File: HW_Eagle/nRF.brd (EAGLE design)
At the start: 44.4 x 39.9 mm, 24 parts, among them X1 B4B-ZR

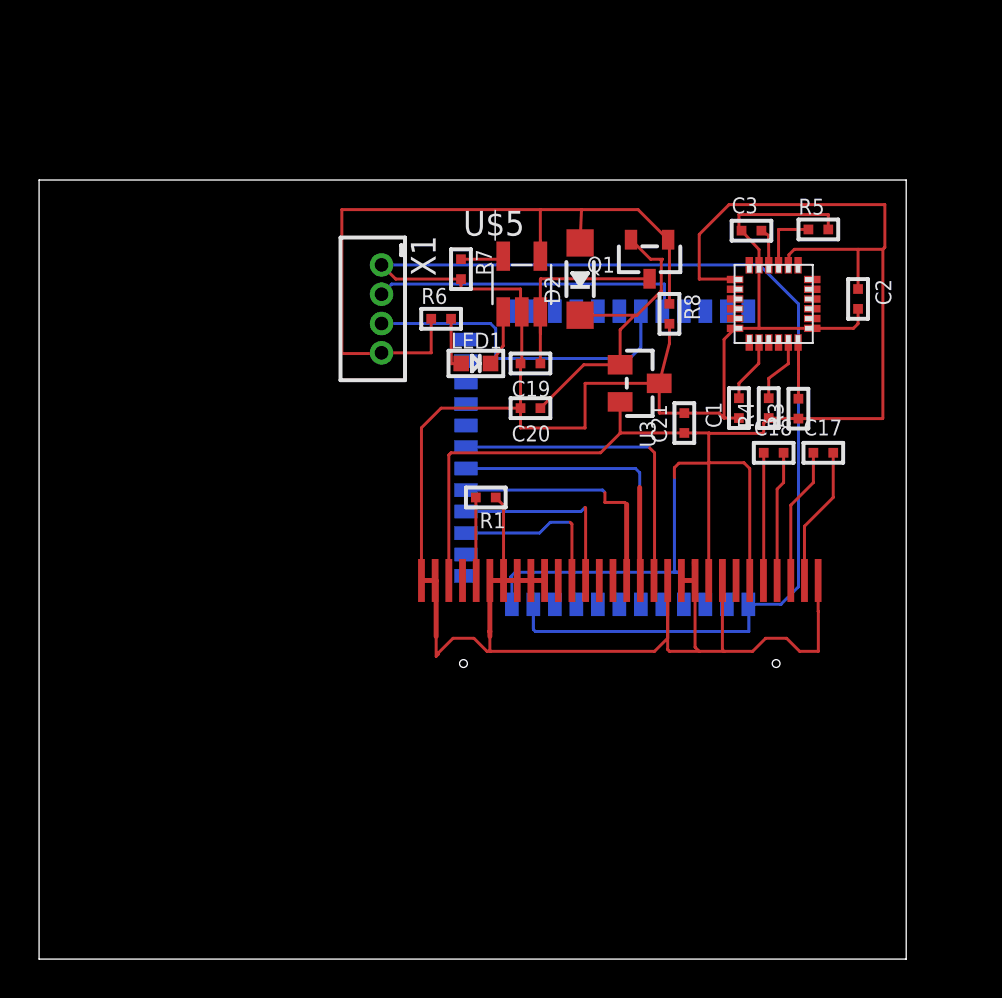
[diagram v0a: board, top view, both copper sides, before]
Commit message: [HW] Add Batterry connector
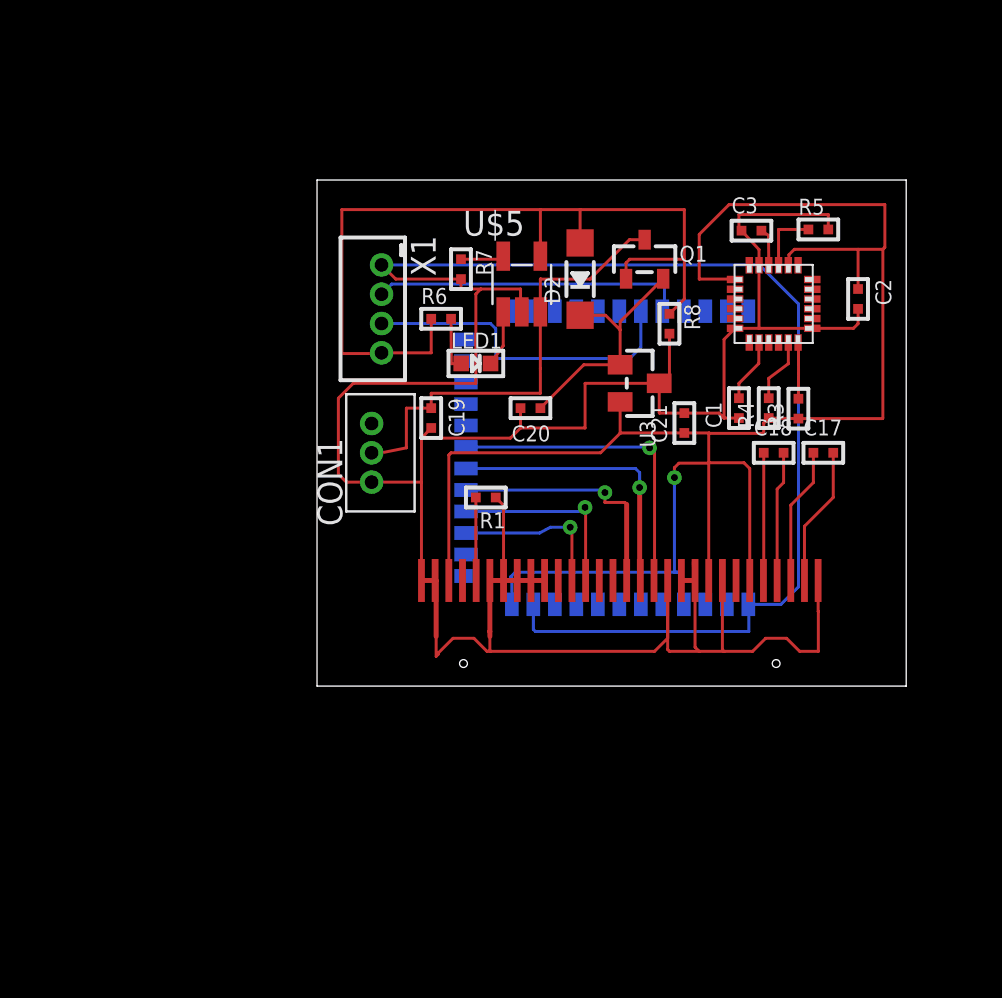
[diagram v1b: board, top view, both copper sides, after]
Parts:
- added CON1: B3B-ZR, jst:B3B-ZR
- moved C19 5.80 mm to (22.1, 55.1), turned to 270 degrees
- moved R8 0.51 mm to (34.3, 59.9)
- moved Q1 0.25 mm to (33.0, 63.2), turned to 0 degrees
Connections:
- net GND: now also CON1.1
- net VBAT: now also CON1.2
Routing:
- net GND: track 179.5 -> 194.9 mm
- net VBAT: track 11.0 -> 23.5 mm
- net N$15: track 39.2 -> 45.6 mm
- net N$25: track 16.2 -> 12.7 mm
- net MOSI: track 8.58 -> 8.48 mm, vias 0 -> 1
- net VCC: vias 0 -> 1
- net SCK: vias 0 -> 1
- net RES: vias 0 -> 1
- net DC: vias 0 -> 1
- net CS: vias 0 -> 1
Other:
- board size 44.4 x 39.9 mm -> 30.1 x 25.9 mm

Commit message: [HW] Change to using modules
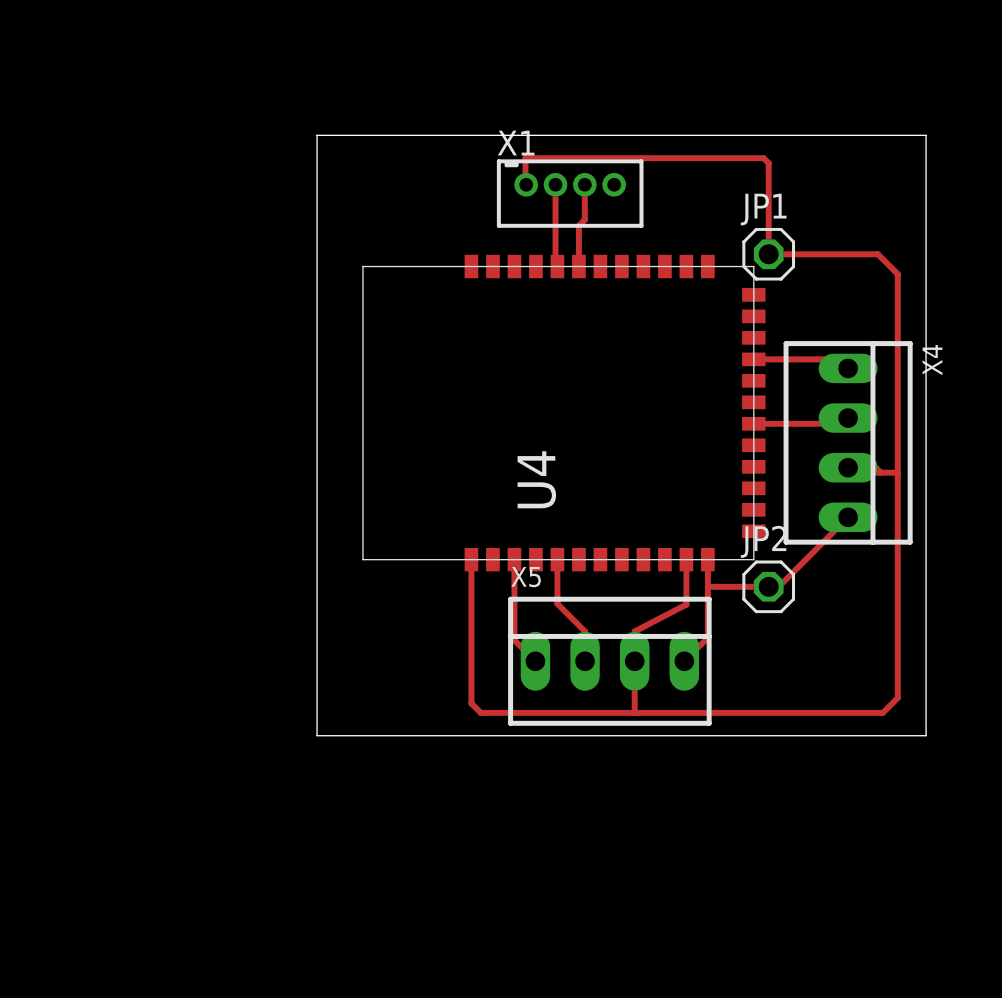
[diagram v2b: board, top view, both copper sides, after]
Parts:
- removed C1, C17, C18, C19, C2, C20, C21, C3: (no value), rc-master-smd:C0402
- removed CON1: B3B-ZR, jst:B3B-ZR
- removed D2: (no value), microbuilder:SOD-123
- removed LED1: (no value), microbuilder:CHIPLED_0603
- removed Q1: (no value), microbuilder:SOT23-R
- removed R1, R3, R4, R5, R6, R7, R8: (no value), rc-master-smd:R0402
- removed U$3: MPU-6050, invensense:QFN.24.4X4
- removed U$5: MCP73832SMD-W, NicShackle:SOT-23-5
- removed U2: (no value), microbuilder:UG-2864HSWEG01_0.96IN_WRAPAROUND
- removed U3: (no value), microbuilder:SOT23-WIDE
- added JP1, JP2: (no value), pinhead:1X01
- added X4, X5: 22-23-2041, con-molex:22-23-2041
- moved U4 14.9 mm to (38.6, 55.4), flipped to the top
- moved X1 11.6 mm to (29.2, 67.1), turned to 0 degrees
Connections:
- removed net CS: U2.13, U4.P.05
- removed net DC: U2.15, U4.P.03
- removed net MOSI: U2.19, U4.P.01
- removed net N$13: R5.1, U$3.9
- removed net N$14: C3.2, U$3.10
- removed net N$15: D2.A, Q1.1, R6.1, R8.1, U$5.4, X1.4
- removed net N$16: LED1.C, U$5.1
- removed net N$17: C17.2, U2.2
- removed net N$18: C1.2, U$3.20
- removed net N$19: C18.2, U2.4
- removed net N$20: C17.1, U2.3
- removed net N$21: C18.1, U2.5
- removed net N$22: R1.2, U2.26
- removed net N$23: LED1.A, R6.2
- removed net N$24: R7.1, U$5.5
- removed net N$25: C20.1, D2.C, Q1.2, U3.1
- removed net RES: U2.14, U4.P.04
- removed net SCK: U2.18, U4.P.02
- removed net SCL: R4.2, U$3.23
- removed net SDA: R3.2, U$3.24
- removed net VBAT: C19.1, CON1.2, Q1.3, U$5.3
- new net MPU6050_SCL: U4.P.04, X4.2
- new net MPU6050_SDA: U4.P.07, X4.1
- new net OLED_SCL: U4.P.24, X5.2
- new net OLED_SDA: U4.P.22, X5.1
- net GND: now also JP1.1, X4.3, X5.3; no longer C1.1, C19.2, C2.2, C20.2, C21.2, C3.1, CON1.1, R1.1, R5.2, R7.2, R8.2, U$3.1, U$3.11, U$3.18, U$5.2, U2.1, U2.10, U2.11, U2.12, U2.21, U2.22, U2.23, U2.24, U2.25, U2.29, U2.30, U2.8, U3.3
- net VCC: now also JP2.1, X4.4, X5.4; no longer C2.1, C21.1, R3.1, R4.1, U$3.13, U$3.8, U2.28, U2.6, U2.9, U3.2
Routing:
- net GND: track 194.9 -> 90.9 mm
- net VCC: track 97.2 -> 14.3 mm, vias 1 -> 0
- net N$15: track 45.6 -> 0.00 mm
- net VBAT: track 23.5 -> 0.00 mm
- net CS: track 16.3 -> 0.00 mm, vias 1 -> 0
- net RES: track 14.5 -> 0.00 mm, vias 1 -> 0
- net DC: track 12.7 -> 0.00 mm, vias 1 -> 0
- net SWDIO: track 17.0 -> 4.31 mm
- net N$25: track 12.7 -> 0.00 mm
- net SWDCLK: track 16.1 -> 4.22 mm
- net SCK: track 9.93 -> 0.00 mm, vias 1 -> 0
- net MOSI: track 8.48 -> 0.00 mm, vias 1 -> 0
- net N$17: track 7.14 -> 0.00 mm
- net N$20: track 7.01 -> 0.00 mm
- net N$19: track 6.67 -> 0.00 mm
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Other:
- board size 30.1 x 25.9 mm -> 31.2 x 30.7 mm

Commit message: Add regulator
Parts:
- added C1, C2: (no value), rcl:C0805
- added P1: (no value), Voltage Regulator:SOT-89
- moved X4 3.21 mm to (44.5, 56.9), flipped to the bottom, turned to 90 degrees
- moved JP1 2.50 mm to (40.7, 61.4)
- moved JP2 1.69 mm to (40.9, 47.2)
- moved U4 1.48 mm to (37.8, 54.1)
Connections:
- new net V_BAT: C2.1, JP2.1, P1.2
- net GND: now also C1.2, C2.2, P1.1
- net MPU6050_SCL: now also X4.1; no longer X4.2
- net MPU6050_SDA: now also X4.2; no longer X4.1
- net VCC: now also C1.1, P1.3; no longer JP2.1
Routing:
- net VCC: track 14.3 -> 41.3 mm
- net GND: track 90.9 -> 104.3 mm
- net V_BAT: track 0.00 -> 6.75 mm
- net MPU6050_SCL: track 4.95 -> 8.34 mm
- net MPU6050_SDA: track 5.02 -> 7.11 mm
- net SWDIO: track 4.31 -> 5.90 mm
- net SWDCLK: track 4.22 -> 5.73 mm
- net OLED_SDA: track 5.64 -> 4.69 mm
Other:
- board size 31.2 x 30.7 mm -> 32.7 x 30.7 mm

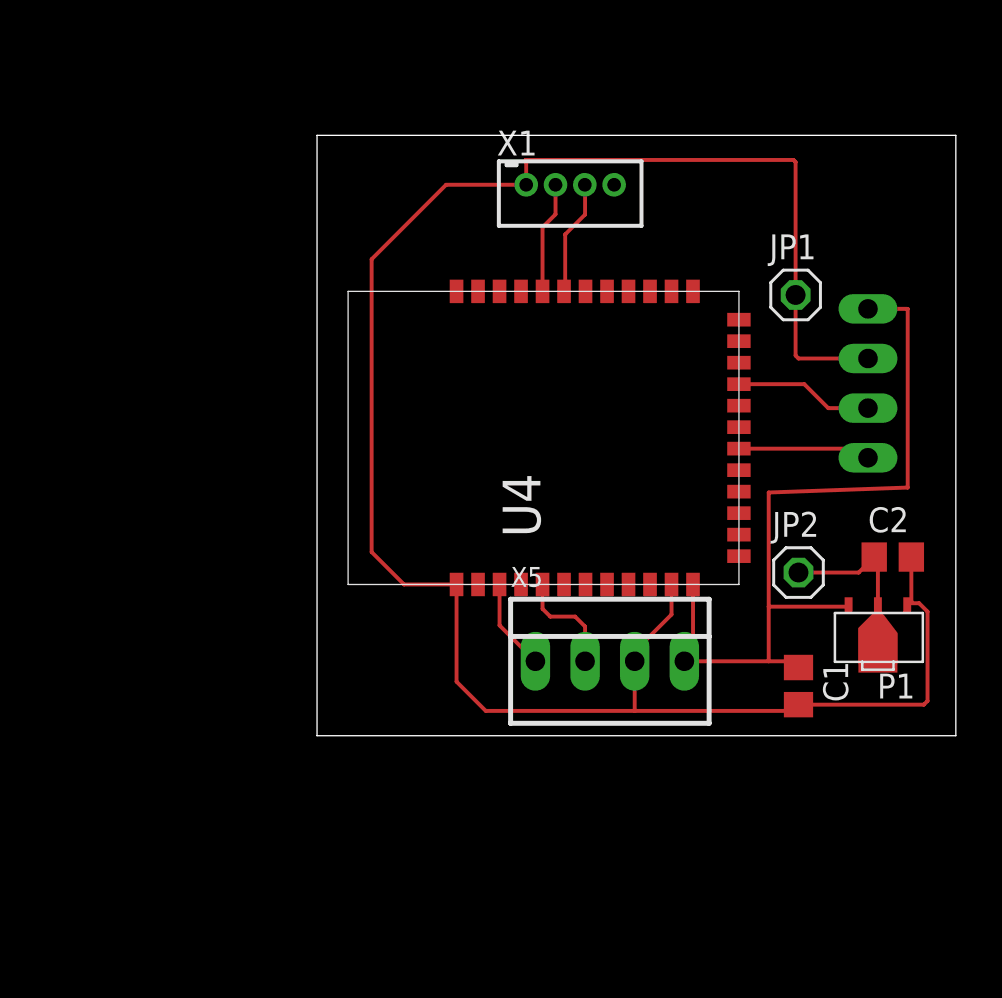
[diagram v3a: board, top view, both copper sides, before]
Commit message: Change LDO package
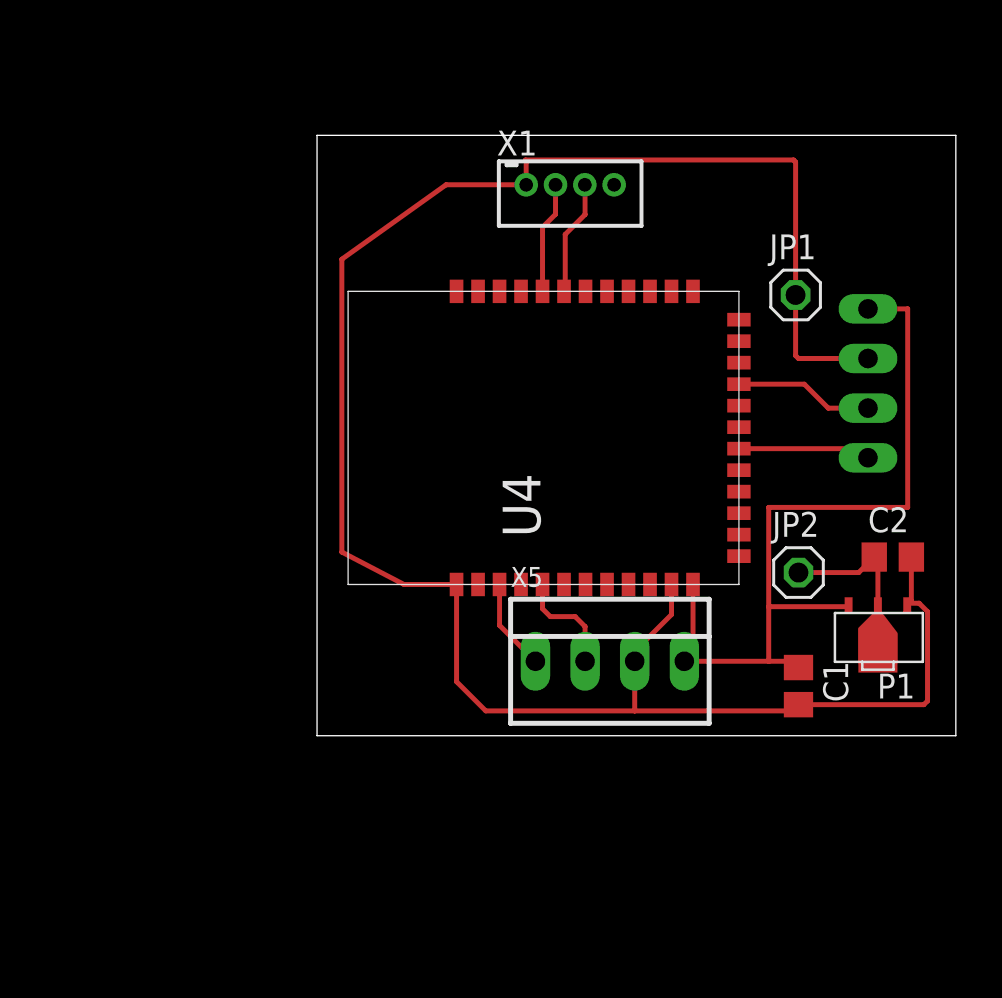
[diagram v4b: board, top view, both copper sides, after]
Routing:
- net GND: track 104.3 -> 106.7 mm
- net MPU6050_SCL: track 8.34 -> 6.80 mm

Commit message: [HW] Add modules: Oled, MPU6050, TP4056
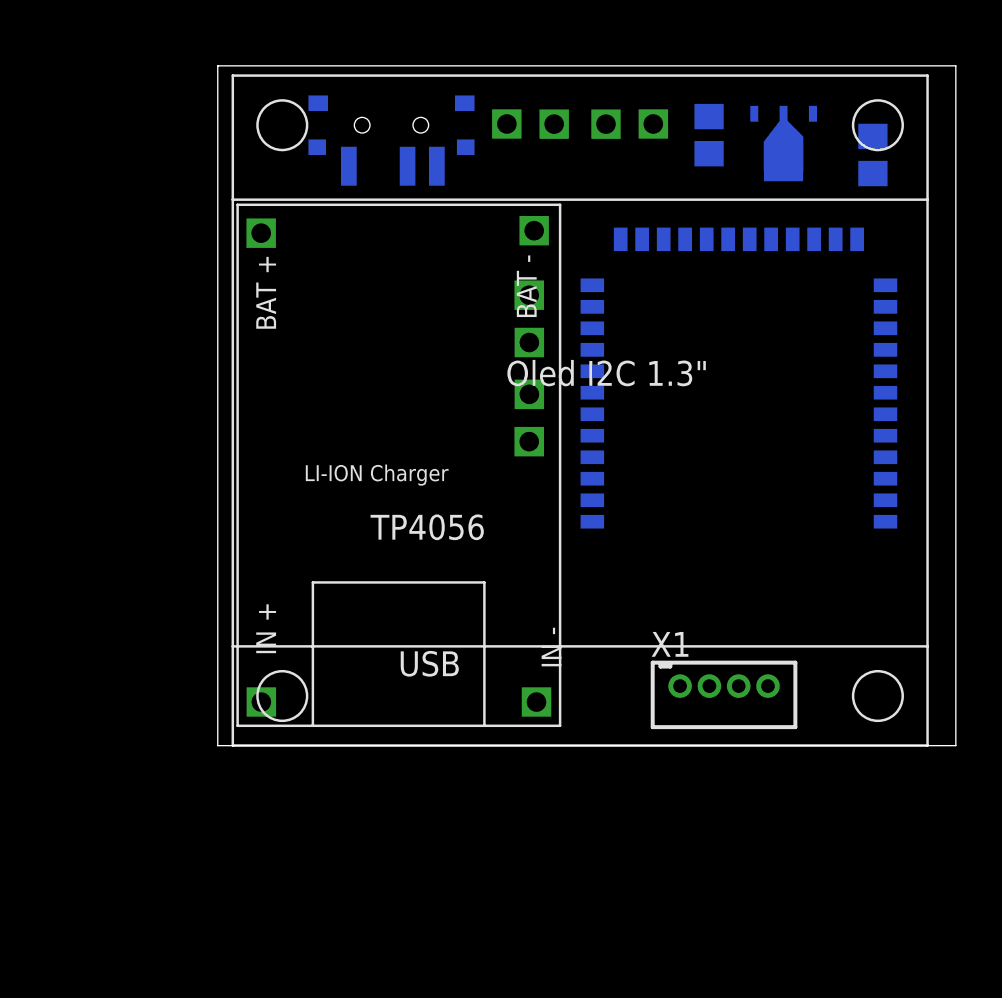
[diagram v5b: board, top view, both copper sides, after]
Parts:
- removed JP1, JP2: (no value), pinhead:1X01
- removed X4, X5: 22-23-2041, con-molex:22-23-2041
- added U$1: MSK-12C02_SMD_SPDT_SWITCH, MSK-12C02 SMD Micro Slider Switch SPDT 2:MSK-12C02
- added U$2: TP4056, TP4056 charging module:TP4056
- added U$3: OLED, Oled:OLED_1.3_I2C
- added U$4: MPU60XX, 6050:MPU6050
- moved C1 28.6 mm to (36.3, 69.6), flipped to the bottom
- moved X1 26.8 mm to (37.1, 41.4)
- moved P1 25.6 mm to (40.1, 69.1), flipped to the bottom
- moved C2 20.6 mm to (44.7, 68.6), flipped to the bottom, turned to 270 degrees
- moved U4 10.2 mm to (37.8, 64.3), flipped to the bottom, turned to 180 degrees
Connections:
- new net N$1: U$1.COM, U$2.BAT+
- net GND: now also U$2.BAT-, U$3.GND, U$4.GND; no longer JP1.1, X4.3, X5.3
- net MPU6050_SCL: now also U$4.SCK; no longer X4.1
- net MPU6050_SDA: now also U$4.SDA; no longer X4.2
- net OLED_SCL: now also U$3.SCK; no longer X5.2
- net OLED_SDA: now also U$3.SDA; no longer X5.1
- net VCC: now also U$3.VCC, U$4.VCC; no longer X4.4, X5.4
- net V_BAT: now also U$1.L2; no longer JP2.1
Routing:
- net GND: track 106.7 -> 0.00 mm
- net VCC: track 41.6 -> 0.00 mm
- net MPU6050_SDA: track 7.11 -> 0.00 mm
- net MPU6050_SCL: track 6.80 -> 0.00 mm
- net V_BAT: track 6.75 -> 0.00 mm
- net SWDIO: track 5.90 -> 0.00 mm
- net SWDCLK: track 5.73 -> 0.00 mm
- net OLED_SCL: track 5.58 -> 0.00 mm
- net OLED_SDA: track 4.69 -> 0.00 mm
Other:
- board size 32.7 x 30.7 mm -> 37.8 x 34.8 mm

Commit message: [HW] Update HW v1.2
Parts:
- removed U$2: TP4056, TP4056 charging module:TP4056
- removed U4: (no value), YJ-14015:YJ-14015
- added C3: (no value), rcl:C0603
- added R1: (no value), rcl:R0603
- added TS-3625-W: MOMENTARY-SWITCH-SPST-SMD-6.0X3.5MM, SparkFun-Switches:TACTILE_SWITCH_SMD_6.0X3.5MM
- added U$5: NRF51822, nrf51822:NRF51822_HSHOP
- added U$6: TP4056, TP4056 charging module:TP4056
- moved C2 31.7 mm to (17.5, 52.3), flipped to the top, turned to 0 degrees
- moved X1 29.1 mm to (40.1, 70.4), turned to 180 degrees
- moved P1 27.4 mm to (15.5, 57.1), flipped to the top, turned to 0 degrees
- moved U$1 24.8 mm to (14.2, 46.0), flipped to the top, turned to 270 degrees
- moved C1 21.7 mm to (16.0, 62.0), flipped to the top, turned to 180 degrees
- moved U$4 19.9 mm to (40.4, 51.3)
- moved U$3 0.57 mm to (27.7, 60.2)
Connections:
- new net BUTTON: C3.1, R1.1, TS-3625-W.2, U$5.P$13
- net GND: now also C3.2, TS-3625-W.1, U$5.P$11, U$6.BAT-; no longer U$2.BAT-, U4.GND, U4.GND@2
- net MPU6050_SCL: now also U$5.P$17; no longer U4.P.04
- net MPU6050_SDA: now also U$5.P$15; no longer U4.P.07
- net N$1: now also U$6.BAT+; no longer U$2.BAT+
- net OLED_SCL: now also U$5.P$5; no longer U4.P.24
- net OLED_SDA: now also U$5.P$3; no longer U4.P.22
- net SWDCLK: now also U$5.P$24; no longer U4.SWDCLK
- net SWDIO: now also U$5.P$23; no longer U4.SWDIO
- net VCC: now also R1.2, U$5.P$12; no longer U4.VDD
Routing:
- net GND: track 0.00 -> 126.6 mm
- net VCC: track 0.00 -> 83.8 mm
- net OLED_SDA: track 0.00 -> 36.8 mm
- net OLED_SCL: track 0.00 -> 30.0 mm
- net SWDIO: track 0.00 -> 17.2 mm
- net SWDCLK: track 0.00 -> 14.7 mm
- net BUTTON: track 0.00 -> 13.6 mm
- net N$1: track 0.00 -> 11.8 mm
- net MPU6050_SDA: track 0.00 -> 9.98 mm
- net MPU6050_SCL: track 0.00 -> 9.94 mm
- net V_BAT: track 0.00 -> 7.98 mm
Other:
- board size 37.8 x 34.8 mm -> 38.3 x 37.6 mm
